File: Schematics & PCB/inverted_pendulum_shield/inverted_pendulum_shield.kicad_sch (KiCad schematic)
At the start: 38 parts, among them J2 Screw_Terminal_01x04, J3 Screw_Terminal_01x02, J4 Screw_Terminal_01x02, J5 FCR7350R, J6 FCR7350B, Q1 PMOS, SW1 SW_Push, U1 DRV8231DDAR, U3 AP63301WU-7, U4 AP63301WU-7

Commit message: Finished schematic and started on the footprints and parts list
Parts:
- C1: footprint (none) -> Capacitor_SMD:C_0805_2012Metric
- C10: value 2x22uF -> 2x22uF (47uF); footprint (none) -> Capacitor_SMD:C_0805_2012Metric
- C2: footprint (none) -> Capacitor_THT:C_Radial_D5.0mm_H11.0mm_P2.00mm
- C3: renamed from C5; footprint (none) -> Capacitor_SMD:C_0805_2012Metric
- C4: renamed from C8; footprint (none) -> Capacitor_SMD:C_0805_2012Metric
- C5: renamed from C3; footprint (none) -> Capacitor_SMD:C_0805_2012Metric
- C6: renamed from C4; footprint (none) -> Capacitor_SMD:C_0603_1608Metric
- C7: renamed from C6; value 2x22uF -> 2x22uF (47uF); footprint (none) -> Capacitor_SMD:C_0805_2012Metric
- C8: renamed from C7; footprint (none) -> Capacitor_SMD:C_0805_2012Metric
- C9: footprint (none) -> Capacitor_SMD:C_0603_1608Metric
- J1: renamed from J3; footprint (none) -> TerminalBlock:TerminalBlock_MaiXu_MX126-5.0-02P_1x02_P5.00mm
- J2: renamed from J4; footprint (none) -> TerminalBlock:TerminalBlock_MaiXu_MX126-5.0-02P_1x02_P5.00mm
- J3: renamed from J2; footprint (none) -> TerminalBlock:TerminalBlock_MaiXu_MX126-5.0-04P_1x04_P5.00mm
- R1: renamed from R22; value 0.18 -> 0.169; footprint Resistor_SMD:R_0603_1608Metric -> Resistor_SMD:R_1206_3216Metric
- R10: renamed from R19; footprint Resistor_SMD:R_0603_1608Metric -> Resistor_SMD:R_0805_2012Metric
- R11: renamed from R21; footprint Resistor_SMD:R_0603_1608Metric -> Resistor_SMD:R_0805_2012Metric
- R2: renamed from R16; footprint Resistor_SMD:R_0603_1608Metric -> (none)
- R3: renamed from R18; footprint Resistor_SMD:R_0603_1608Metric -> (none)
- R4: renamed from R15; footprint Resistor_SMD:R_0603_1608Metric -> (none)
- R5: renamed from R17; footprint Resistor_SMD:R_0603_1608Metric -> (none)
- R6: renamed from R13; footprint Resistor_SMD:R_0603_1608Metric -> (none)
- R7: renamed from R14; footprint Resistor_SMD:R_0603_1608Metric -> (none)
- R8: renamed from R12; footprint Resistor_SMD:R_0603_1608Metric -> Resistor_SMD:R_0805_2012Metric
- R9: renamed from R20; footprint Resistor_SMD:R_0603_1608Metric -> Resistor_SMD:R_0805_2012Metric
- renumbered D3 to D1, D4 to D2, D5 to D3, J5 to J4, J6 to J5, U3 to U2, U4 to U3
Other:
- note added: "Current is regulated at 2.96A = VREF / (10 * 0.169)"
- note added: "Raspberry Pi Pico connections"
- note removed: "Current is regulated at 2.78A = VREF / (10 * 0.18)"
- note removed: "Might need higher in case of H bridge Vdrop"
- title: (none) -> Reaction-Wheel-Inverted-Pendulum Shield 
- moved on the sheet: A1, D1, J4, J5, Q1, R5

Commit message: Finished schematic and completed ERC
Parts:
- removed SW1: SW_Push, symbol Switch:SW_Push
- added SW1: 1825027, switches:SW_THT_1825027-G_TEC, symbol my_switches:Right angle Tact Switch 2-1825027-0
- D1: footprint (none) -> Diode_SMD:D_SOD-323
- D2, D3: footprint (none) -> LED_THT:LED_D10.0mm
- J4: footprint (none) -> Connector:Banana_Cliff_FCR7350R_S16N-PC_Horizontal
- J5: footprint (none) -> Connector:Banana_Cliff_FCR7350B_S16N-PC_Horizontal
- L1: footprint (none) -> Inductor_SMD:L_TDK_SLF7045
- L2: footprint (none) -> Inductor_SMD:L_Bourns-SRU1028_10.0x10.0mm
- Q1: value PMOS -> FQD8P10TM; footprint (none) -> Package_TO_SOT_SMD:TO-252-3_TabPin2
- R2, R3, R4: footprint (none) -> Resistor_SMD:R_0805_2012Metric
- R5: value ? -> 10k; footprint (none) -> Resistor_SMD:R_0805_2012Metric
- R6, R7: value ? -> 1k; footprint (none) -> Resistor_SMD:R_0805_2012Metric
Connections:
- net Controls Start: now also SW1.1
- net GND: now also A1.33 (AGND), SW1.2, SW1.3, SW1.4
- no-connect marks 21 -> 20
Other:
- note added: "Bench supply will connect to J4 and J5"
- note added: "ERC"
- note added: "need to get footprint for pot"
- moved on the sheet: C10, C3, C4, C5, C6, C7, C8, C9, D1, D2, D3, J1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

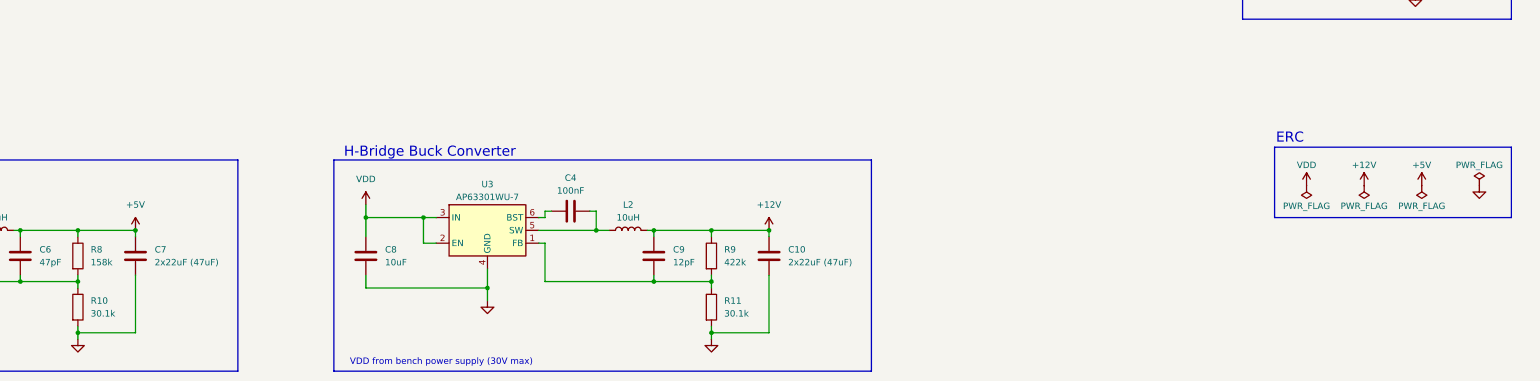
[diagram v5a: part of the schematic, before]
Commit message: Made initial pcb layout without wiring
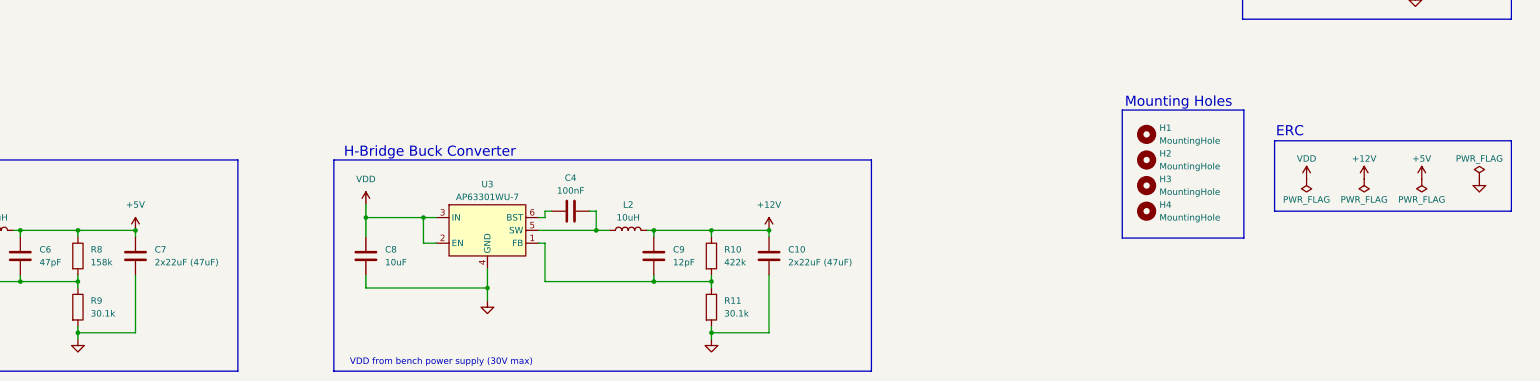
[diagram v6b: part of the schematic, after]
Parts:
- added H1, H2, H3, H4: MountingHole, MountingHole:MountingHole_2.2mm_M2, symbol Mechanical:MountingHole
- renumbered R9 to R10, R10 to R9
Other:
- note added: "Mounting Holes"

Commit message: Finished PCB
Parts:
- H1, H2, H3, H4: footprint MountingHole:MountingHole_2.2mm_M2 -> MountingHole:MountingHole_3.2mm_M3
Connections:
- net Controls Start: now also A1.21 (GPIO16); no longer A1.20 (GPIO15)
- net IMU_INT: now also A1.5 (GPIO3); no longer A1.25 (GPIO19)
- net IMU_RST: now also A1.4 (GPIO2); no longer A1.24 (GPIO18)
- net IMU_SCL: now also A1.10 (GPIO7); no longer A1.27 (GPIO21)
- net IMU_SDA: now also A1.9 (GPIO6); no longer A1.26 (GPIO20)
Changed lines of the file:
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@@
 	)
 	(no_connect
+		(at 233.68 127)
+	)
+	(no_connect
 		(at 187.96 111.76)
 	)
@@
 	)
 	(no_connect
-		(at 187.96 127)
-	)
-	(no_connect
 		(at 187.96 114.3)
 	)
@@
 	)
 	(no_connect
-		(at 187.96 124.46)
+		(at 187.96 139.7)
 	)
 	(no_connect
-		(at 187.96 139.7)
+		(at 187.96 142.24)
 	)
 	(no_connect
-		(at 187.96 137.16)
+		(at 187.96 157.48)
 	)
 	(no_connect
-		(at 187.96 142.24)
+		(at 233.68 132.08)
 	)
 	(no_connect
@@
 	)
 	(no_connect
+		(at 233.68 129.54)
+	)
+	(no_connect
 		(at 233.68 149.86)
 	)
@@
 	)
 	(no_connect
-		(at 233.68 121.92)
-	)
-	(no_connect
 		(at 187.96 154.94)
 	)
 	(no_connect
-		(at 187.96 134.62)
+		(at 233.68 134.62)
 	)
 	(wire
@@
 	(wire
 		(pts
-			(xy 185.42 157.48) (xy 187.96 157.48)
+			(xy 233.68 121.92) (xy 237.49 121.92)
 		)
 		(stroke
@@
 	(wire
 		(pts
-			(xy 233.68 129.54) (xy 237.49 129.54)
+			(xy 205.74 248.92) (xy 208.28 248.92)
 		)
 		(stroke
@@
 	(wire
 		(pts
-			(xy 205.74 248.92) (xy 208.28 248.92)
+			(xy 364.49 191.77) (xy 368.3 191.77)
 		)
 		(stroke
@@
 	(wire
 		(pts
-			(xy 364.49 191.77) (xy 368.3 191.77)
+			(xy 195.58 245.11) (xy 196.85 245.11)
 		)
 		(stroke
@@
 	(wire
 		(pts
-			(xy 195.58 245.11) (xy 196.85 245.11)
+			(xy 58.42 167.64) (xy 58.42 166.37)
 		)
 		(stroke
@@
 	(wire
 		(pts
-			(xy 58.42 167.64) (xy 58.42 166.37)
+			(xy 184.15 134.62) (xy 187.96 134.62)
 		)
 		(stroke
@@
 	(wire
 		(pts
+			(xy 184.15 137.16) (xy 187.96 137.16)
+		)
+		(stroke
+			(width 0)
+			(type default)
+		)
+	)
+	(wire
+		(pts
 			(xy 365.76 140.97) (xy 365.76 138.43)
 		)
@@
 	(wire
 		(pts
+			(xy 184.15 124.46) (xy 187.96 124.46)
+		)
+		(stroke
+			(width 0)
+			(type default)
+		)
+	)
+	(wire
+		(pts
 			(xy 160.02 246.38) (xy 160.02 250.19)
 		)
@@
 	(wire
 		(pts
+			(xy 184.15 127) (xy 187.96 127)
+		)
+		(stroke
+			(width 0)
+			(type default)
+		)
+	)
+	(wire
+		(pts
 			(xy 69.85 251.46) (xy 69.85 259.08)
 		)
@@
 	(wire
 		(pts
-			(xy 233.68 134.62) (xy 238.76 134.62)
-		)
-		(stroke
-			(width 0)
-			(type default)
-		)
-	)
-	(wire
-		(pts
 			(xy 49.53 62.23) (xy 53.34 62.23)
 		)
@@
 	(wire
 		(pts
-			(xy 233.68 127) (xy 237.49 127)
-		)
-		(stroke
-			(width 0)
-			(type default)
-		)
-	)
-	(wire
-		(pts
 			(xy 215.9 93.98) (xy 215.9 96.52)
 		)
@@
 	(wire
 		(pts
-			(xy 233.68 132.08) (xy 238.76 132.08)
-		)
-		(stroke
-			(width 0)
-			(type default)
-		)
-	)
-	(wire
-		(pts
 			(xy 48.26 69.85) (xy 53.34 69.85)
 		)
@@
 	(global_label "IMU_SCL"
 		(shape output)
-		(at 238.76 134.62 0)
+		(at 184.15 137.16 180)
 		(fields_autoplaced yes)
 		(effects
@@
 				(size 1.27 1.27)
 			)
-			(justify left)
+			(justify right)
 		)
 		(property "Intersheetrefs" "${INTERSHEET_REFS}"
-			(at 249.6071 134.62 0)
+			(at 173.3029 137.16 0)
 			(hide yes)
 			(show_name no)
@@
 					(size 1.27 1.27)
 				)
-				(justify left)
+				(justify right)
 			)
 		)
@@
 	(global_label "IMU_RST"
 		(shape input)
-		(at 237.49 127 0)
+		(at 184.15 124.46 180)
 		(fields_autoplaced yes)
 		(effects
@@
 				(size 1.27 1.27)
 			)
-			(justify left)
+			(justify right)
 		)
 		(property "Intersheetrefs" "${INTERSHEET_REFS}"
-			(at 248.2766 127 0)
+			(at 173.3634 124.46 0)
 			(hide yes)
 			(show_name no)
@@
 					(size 1.27 1.27)
 				)
-				(justify left)
+				(justify right)
 			)
 		)
@@
 	(global_label "Controls Start"
 		(shape input)
-		(at 185.42 157.48 180)
+		(at 237.49 121.92 0)
 		(fields_autoplaced yes)
 		(effects
@@
 				(size 1.27 1.27)
 			)
-			(justify right)
+			(justify left)
 		)
 		(property "Intersheetrefs" "${INTERSHEET_REFS}"
-			(at 168.9489 157.48 0)
+			(at 253.9611 121.92 0)
 			(hide yes)
 			(show_name no)
@@
 					(size 1.27 1.27)
 				)
-				(justify right)
+				(justify left)
 			)
 		)
@@
 	(global_label "IMU_INT"
 		(shape input)
-		(at 237.49 129.54 0)
+		(at 184.15 127 180)
 		(fields_autoplaced yes)
 		(effects
@@
 				(size 1.27 1.27)
 			)
-			(justify left)
+			(justify right)
 		)
 		(property "Intersheetrefs" "${INTERSHEET_REFS}"
-			(at 247.7324 129.54 0)
+			(at 173.9076 127 0)
 			(hide yes)
 			(show_name no)
@@
 					(size 1.27 1.27)
 				)
-				(justify left)
+				(justify right)
 			)
 		)
@@
 	(global_label "IMU_SDA"
 		(shape output)
-		(at 238.76 132.08 0)
+		(at 184.15 134.62 180)
 		(fields_autoplaced yes)
 		(effects
@@
 				(size 1.27 1.27)
 			)
-			(justify left)
+			(justify right)
 		)
 		(property "Intersheetrefs" "${INTERSHEET_REFS}"
-			(at 249.6676 132.08 0)
+			(at 173.2424 134.62 0)
 			(hide yes)
 			(show_name no)
@@
 					(size 1.27 1.27)
 				)
-				(justify left)
+				(justify right)
 			)
 		)
@@
 			)
 		)
-		(property "Footprint" "MountingHole:MountingHole_2.2mm_M2"
+		(property "Footprint" "MountingHole:MountingHole_3.2mm_M3"
 			(at 314.96 245.11 0)
 			(hide yes)
@@
 			)
 		)
-		(property "Footprint" "MountingHole:MountingHole_2.2mm_M2"
+		(property "Footprint" "MountingHole:MountingHole_3.2mm_M3"
 			(at 314.96 240.03 0)
 			(hide yes)
@@
 			)
 		)
-		(property "Footprint" "MountingHole:MountingHole_2.2mm_M2"
+		(property "Footprint" "MountingHole:MountingHole_3.2mm_M3"
 			(at 314.96 229.87 0)
 			(hide yes)
@@
 			)
 		)
-		(property "Footprint" "MountingHole:MountingHole_2.2mm_M2"
+		(property "Footprint" "MountingHole:MountingHole_3.2mm_M3"
 			(at 314.96 234.95 0)
 			(hide yes)

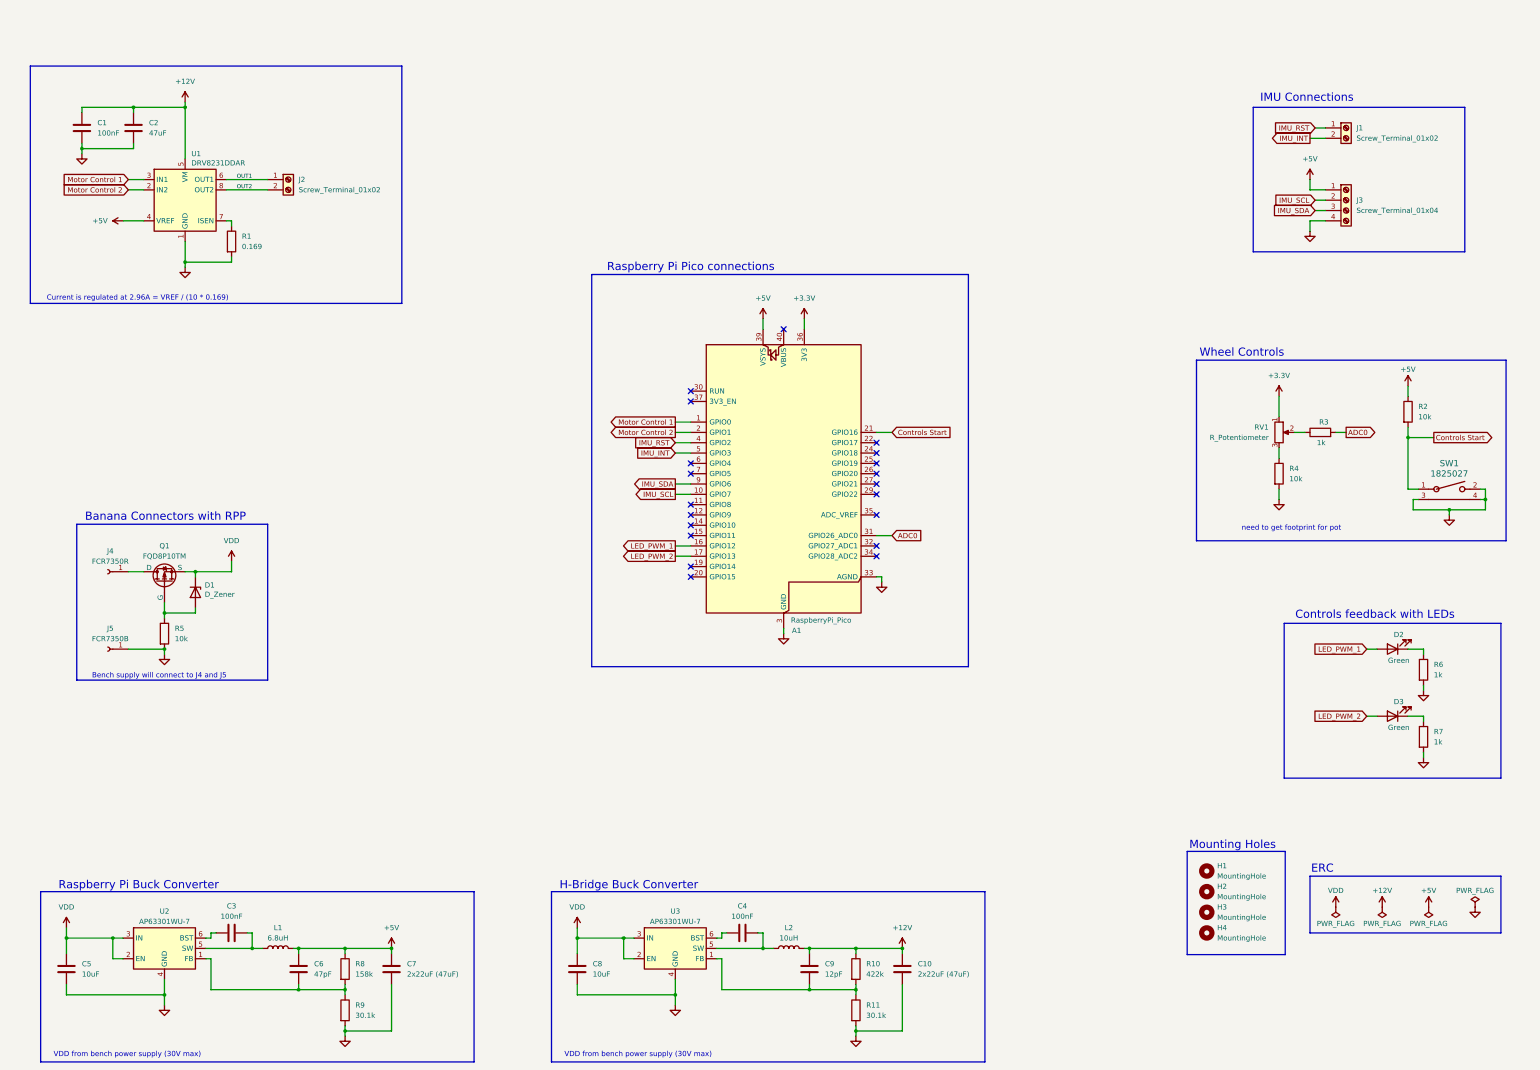
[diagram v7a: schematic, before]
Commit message: Made next revision of schematic and with parts of pcb done
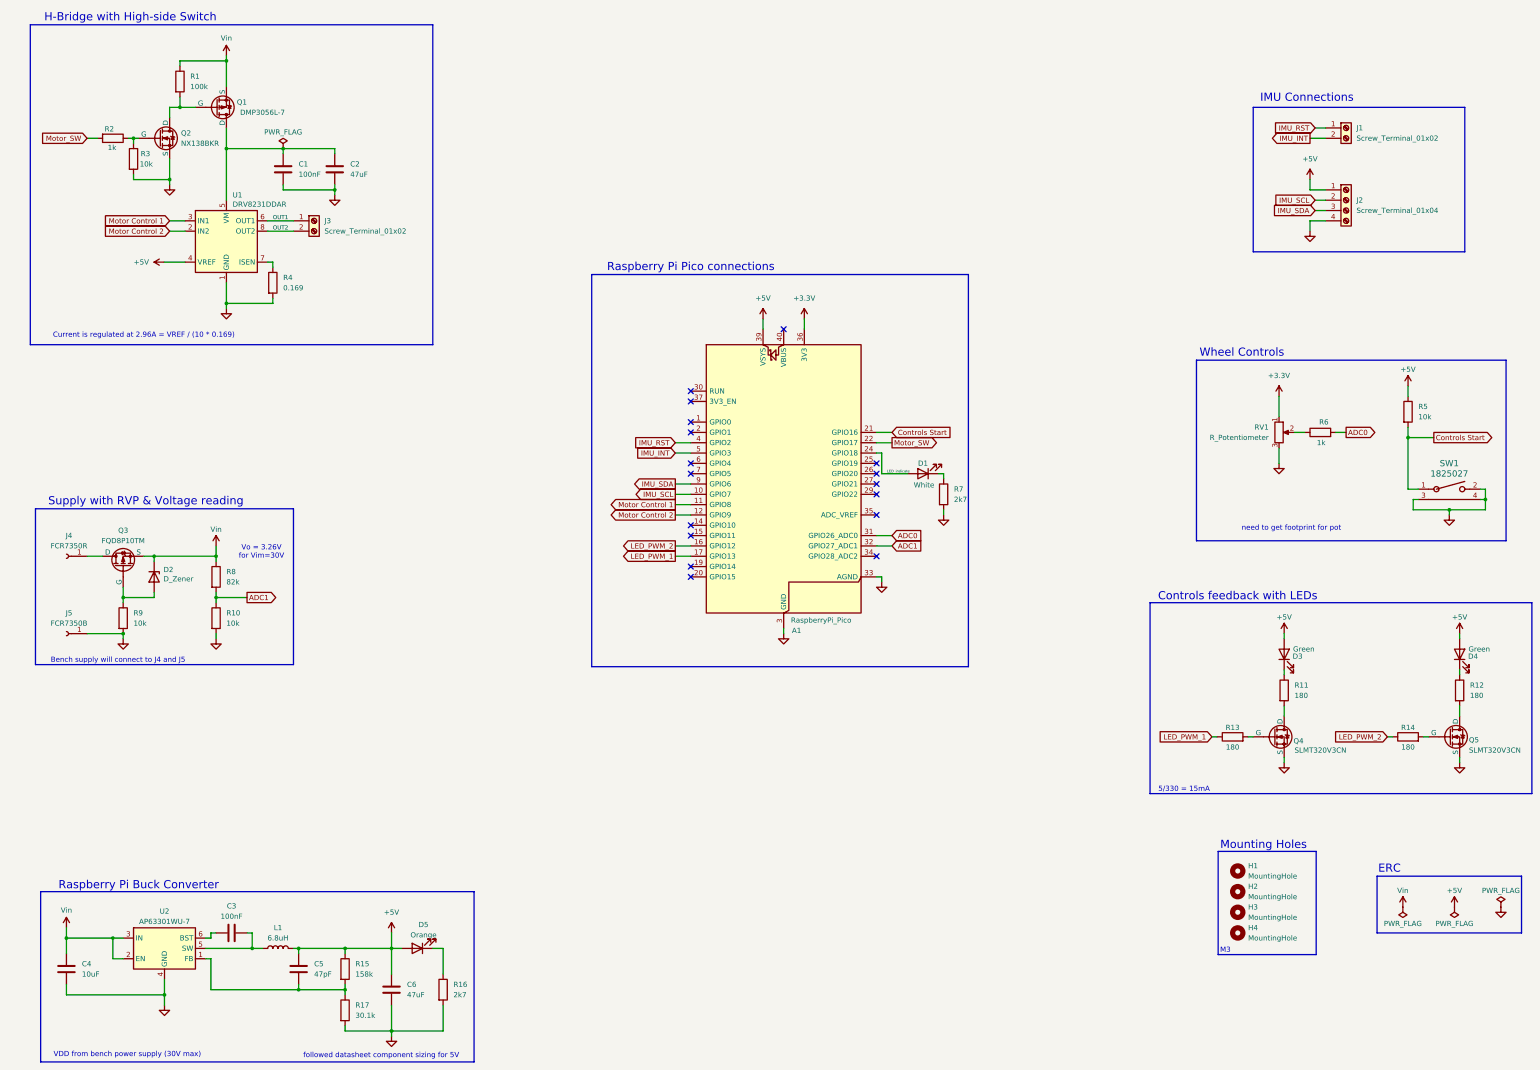
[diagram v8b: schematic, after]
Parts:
- removed C10: 2x22uF (47uF), Capacitor_SMD:C_0805_2012Metric, symbol Device:C
- removed C4: 100nF, Capacitor_SMD:C_0805_2012Metric, symbol Device:C
- removed C8: 10uF, Capacitor_SMD:C_0805_2012Metric, symbol Device:C
- removed C9: 12pF, Capacitor_SMD:C_0603_1608Metric, symbol Device:C
- removed D2: Green, LED_THT:LED_D10.0mm, symbol Device:LED
- removed L2: 10uH, Inductor_SMD:L_Bourns-SRU1028_10.0x10.0mm, symbol Device:L
- removed R11: 30.1k, Resistor_SMD:R_0805_2012Metric, symbol Device:R
- removed R4: 10k, Resistor_SMD:R_0805_2012Metric, symbol Device:R
- removed R6: 1k, Resistor_SMD:R_0805_2012Metric, symbol Device:R
- removed U3: AP63301WU-7, Package_TO_SOT_SMD:TSOT-23-6, symbol Regulator_Switching:AP63201WU
- added D1: White, Resistor_SMD:R_0603_1608Metric, symbol Device:LED
- added D4: Green, LED_THT:LED_D10.0mm, symbol Device:LED
- added D5: Orange, Resistor_SMD:R_0805_2012Metric, symbol Device:LED
- added Q1: DMP3056L-7, Package_TO_SOT_SMD:SOT-23-3, symbol Simulation_SPICE:PMOS
- added Q2: NX138BKR, Package_TO_SOT_SMD:SOT-23, symbol Simulation_SPICE:NMOS
- added Q4, Q5: SLMT320V3CN, Package_TO_SOT_SMD:SOT-23, symbol Simulation_SPICE:NMOS
- added R1: 100k, Resistor_SMD:R_0805_2012Metric, symbol Device:R
- added R12, R13, R14: 180, Resistor_SMD:R_0805_2012Metric, symbol Device:R
- added R16, R7: 2k7, Resistor_SMD:R_0805_2012Metric, symbol Device:R
- added R2: 1k, Resistor_SMD:R_0805_2012Metric, symbol Device:R
- added R3: 10k, Resistor_SMD:R_0805_2012Metric, symbol Device:R
- added R8: 82k, Resistor_SMD:R_0805_2012Metric, symbol Device:R
- A1: footprint Module:RaspberryPi_Pico_Common_Unspecified -> Module:RaspberryPi_Pico_Common_THT
- C6: renamed from C7; value 2x22uF (47uF) -> 47uF
- Q3: renamed from Q1; footprint Package_TO_SOT_SMD:TO-252-3_TabPin2 -> Package_TO_SOT_SMD:TO-252-2_TabPin1
- R10: value 422k -> 10k
- R11: renamed from R7; value 1k -> 180
- RV1: footprint (none) -> pendulum_footprints:uc_potentiometer
- renumbered C5 to C4, C6 to C5, D1 to D2, J3 to J2, J2 to J3, R8 to R15, R9 to R17, R1 to R4, R2 to R5, R3 to R6, R5 to R9
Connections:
- net +5V: now also D3.2 (A), D4.2 (A), D5.2 (A)
- net GND: now also R10.2, RV1.3, Q2.3 (S), Q4.3 (S), Q5.3 (S), R16.2, R3.2, R7.2; no longer R11.2
- net LED_PWM_1: now also A1.17 (GPIO13), R13.1; no longer A1.16 (GPIO12)
- net LED_PWM_2: now also A1.16 (GPIO12), R14.1; no longer A1.17 (GPIO13), D3.2 (A)
- net Motor Control 1: now also A1.11 (GPIO8); no longer A1.1 (GPIO0)
- net Motor Control 2: now also A1.12 (GPIO9); no longer A1.2 (GPIO1)
- net Motor_SW: now reaches A1.22 (GPIO17)
- net Motor_SW: now also R2.2
- net LED_indicate: now reaches A1.24 (GPIO18)
- net LED_indicate: now also D1.2 (A)
- net ADC1: now reaches A1.32 (GPIO27_ADC1)
- net ADC1: now also R10.1, R8.2
- net +12V: no longer names the net of C1.1, C2.1, U1.5 (VM)
- net +12V: now also Q1.1 (D); no longer R10.1
- net VDD renamed Vin
- net Vin: now also Q1.3 (S), R1.1, R8.1
- new net: D5.1 (K), R16.1
- new net: Q4.1 (D), R11.2
- new net: Q4.2 (G), R13.2
- new net: Q1.2 (G), Q2.1 (D), R1.2
- new net: Q2.2 (G), R2.1, R3.1
- new net: D1.1 (K), R7.1
- new net: Q5.2 (G), R14.2
- new net: Q5.1 (D), R12.2
- new net: D4.1 (K), R12.1
- no-connect marks 20 -> 17
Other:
- note added: "5/330 = 15mA"
- note added: "H-Bridge with High-side Switch"
- note added: "M3"
- note added: "Supply with RVP & Voltage reading"
- note added: "Vo = 3.26V for Vim=30V"
- note added: "followed datasheet component sizing for 5V"
- note removed: "Banana Connectors with RPP"
- note removed: "H-Bridge Buck Converter"
- moved on the sheet: C1, C2, C6, D2, D3, H1, H2, H3, H4, J3, J4, J5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
